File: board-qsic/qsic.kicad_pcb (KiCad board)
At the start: 4 copper layers, 214.1 x 131.7 mm, 152 parts, among them CON1 SD 0, CON2 SD 1, J601 USB_A, P2 Indicator Panel, U207 DS8641-LR, U208 74LVC8T245, U209 74LVC8T245, U210 DS8641-LR, U211 DS8641-LR, U212 74LVC8T245, U213 74LVC8T245, U214 DS8641-LR, U215 DS8641-LR, U216 74LVC8T245, U306 AOZ3010PI, U307 AOZ3010PI, U308 RT8288A, U309 SC189, U401 XC7A75T-CSG324, U501 IS43TR16128B, U502 DS8641-LR, U503 74LVC8T245, U504 74LVC8T245, U505 DS8641-LR, U506 DS8641-LR, U507 74LVC8T245, U508 74LVC8T245, U509 DS8641-LR, U510 DS8641-LR, U511 74LVC8T245, U512 74LVC8T245, U513 DS8641-LR, U601 MAX3033E, U602 USB3340

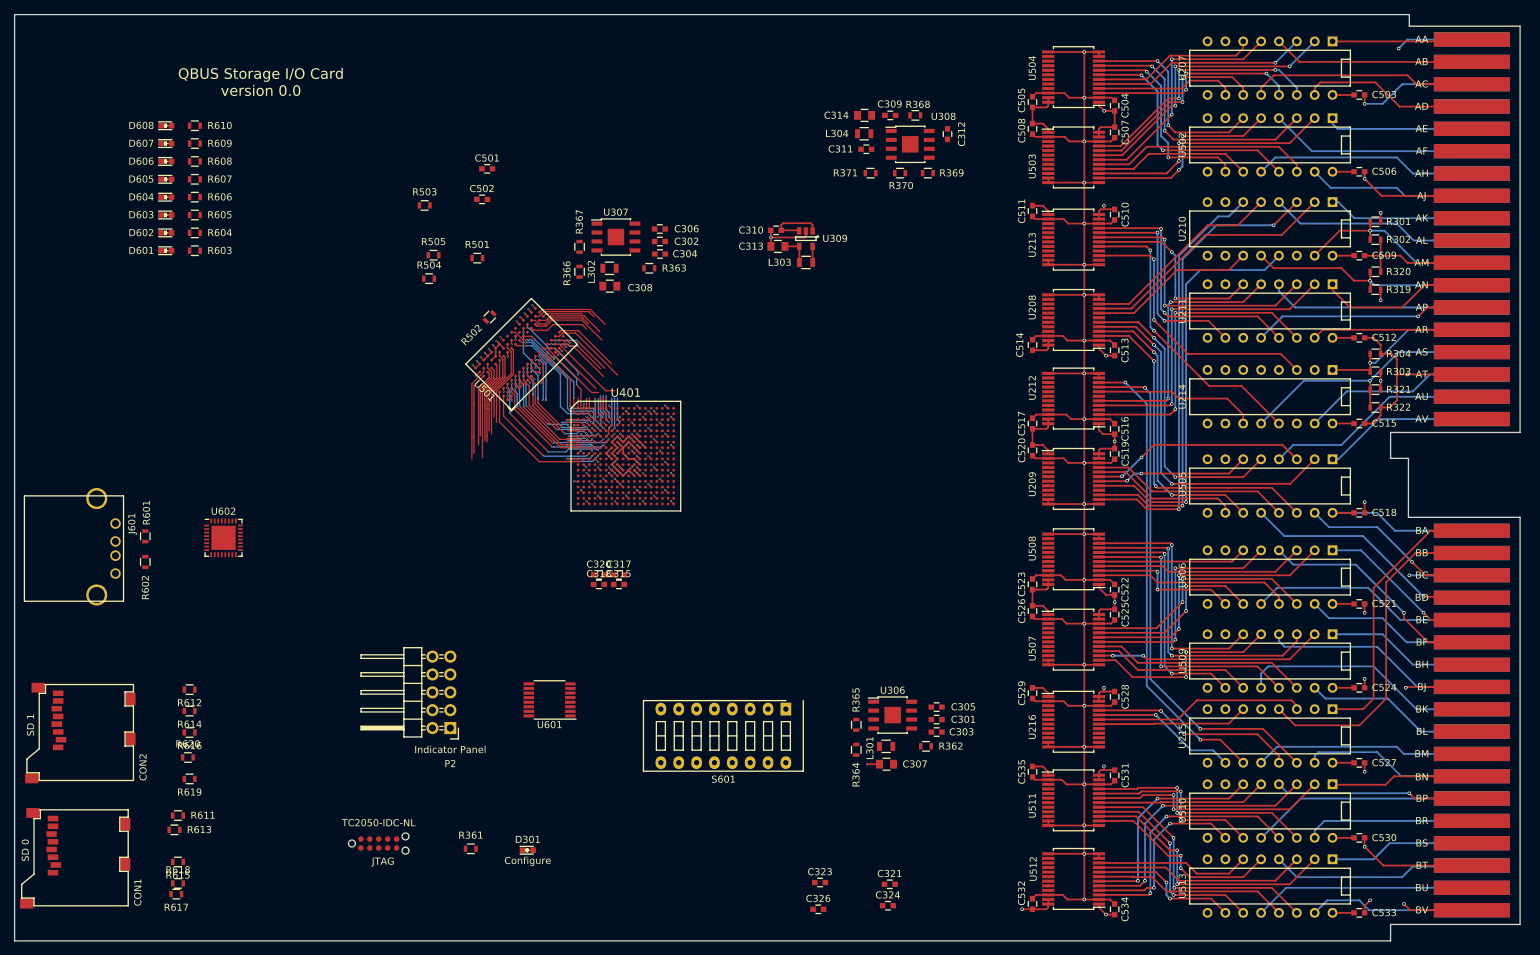
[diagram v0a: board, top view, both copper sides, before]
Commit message: Reworked board from template.  Changed schematic to let me use the bus drivers and level converters more efficiently so to get all the signals.
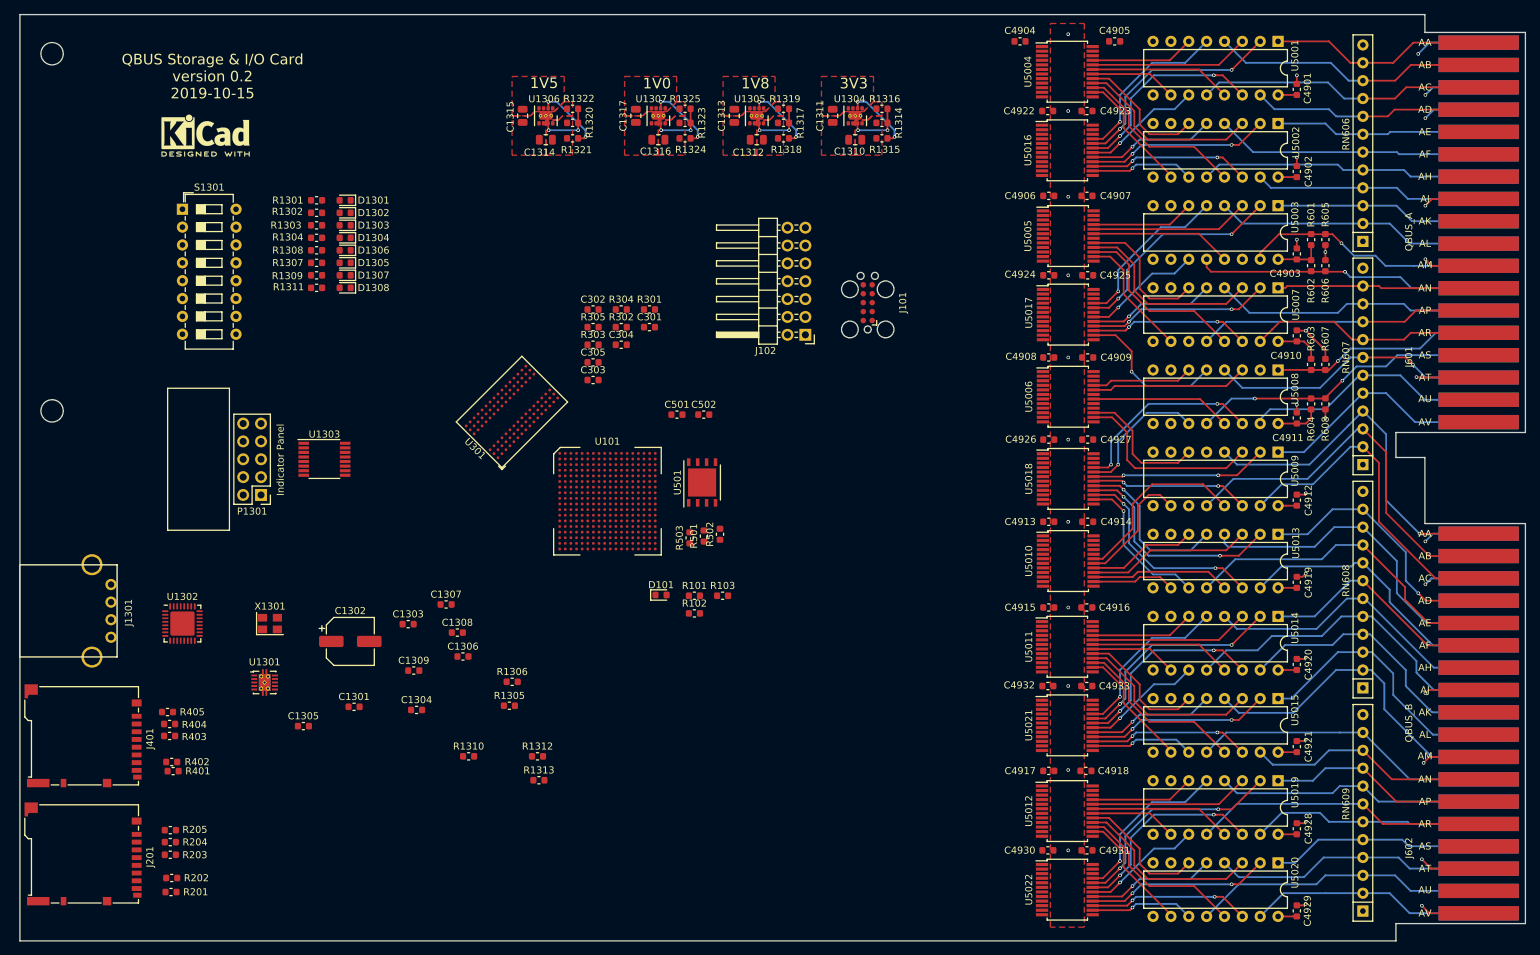
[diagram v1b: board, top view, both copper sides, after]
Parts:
- removed B101: QBUS, myMods.pretty:Qbus-double
- removed C306, C311, C312, C315, C317, C318, C320, C321, C323, C324, C326, C503, C504, C505, C506, C507, C508, C509, C510, C511, C512, C513, C514, C515, C516, C517, C518, C519, C520, C521, C522, C523, C524, C525, C526, C527, C528, C529, C530, C531, C532, C533, C534, C535: 100nF, Capacitors_SMD:C_0603
- removed C307, C308, C313, C314: 22uF, Capacitors_SMD:C_0805
- removed C309, C310: 10uF, Capacitors_SMD:C_0603
- removed CON1: SD 0, myMods.pretty:microSD-3M-2900-series
- removed CON2: SD 1, myMods.pretty:microSD-3M-2900-series
- removed D301: Configure, LEDs:LED-0603
- removed D601: LED 0, LEDs:LED-0603
- removed D602: LED 1, LEDs:LED-0603
- removed D603: LED 2, LEDs:LED-0603
- removed D604: LED 3, LEDs:LED-0603
- removed D605: LED 4, LEDs:LED-0603
- removed D606: LED 5, LEDs:LED-0603
- removed D607: LED 6, LEDs:LED-0603
- removed D608: LED 7, LEDs:LED-0603
- removed JTAG: TC2050-IDC-NL, myMods.pretty:TC2050-IDC-NL
- removed L301, L302: 4.7uH, Resistors_SMD:R_0805
- removed L303: 1.5uH, Resistors_SMD:R_0805
- removed L304: 2.2uH, Resistors_SMD:R_0805
- removed P2: Indicator Panel, Pin_Headers:Pin_Header_Angled_2x05
- removed R319, R321: 330, Resistors_SMD:R_0603
- removed R320, R322: 680, Resistors_SMD:R_0603
- removed R361, R505: 240, Resistors_SMD:R_0603
- removed R362, R363: 7.5k, Resistors_SMD:R_0603
- removed R364: 31.1k, Resistors_SMD:R_0603
- removed R365, R366: 10k, Resistors_SMD:R_0603
- removed R367: 11.5k, Resistors_SMD:R_0603
- removed R368: 100k, Resistors_SMD:R_0603
- removed R369, R611, R612, R613, R614, R615, R616, R617, R619: 50k, Resistors_SMD:R_0603
- removed R370: 18.2k, Resistors_SMD:R_0603
- removed R371: 4.7k, Resistors_SMD:R_0603
- removed R504: 47, Resistors_SMD:R_0603
- removed R609, R610: R, Resistors_SMD:R_0603
- removed R618, R620: 270k, Resistors_SMD:R_0603
- removed the REF** at (34.0, 55.9)
- removed S601: Config, Buttons_Switches_ThroughHole:SW_DIP_x8_Slide
- removed U207, U210, U211, U214, U215, U502, U505, U506, U509, U510, U513: DS8641-LR, Housings_DIP:DIP-16__300
- removed U208, U209, U212, U213, U216, U503, U504, U507, U508, U511, U512: 74LVC8T245, Housings_SSOP:SSOP-24_5.3x8.2mm_Pitch0.65mm
- removed U306, U307: AOZ3010PI, Housings_SOIC:SOIC-8-1EP_3.9x4.9mm_Pitch1.27mm
- removed U308: RT8288A, Housings_SOIC:SOIC-8-1EP_3.9x4.9mm_Pitch1.27mm
- removed U309: SC189, TO_SOT_Packages_SMD:SOT-23-5
- removed U401: XC7A75T-CSG324, myMods.pretty:CSG324
- removed U601: MAX3033E, Housings_SSOP:TSSOP-16_4.4x5mm_Pitch0.65mm
- removed U602: USB3340, Housings_DFN_QFN:QFN-32-1EP_5x5mm_Pitch0.5mm
- added C1301: 100nF, Capacitor_SMD:C_0603_1608Metric, F.Cu at (80.5, 123.9)
- added C1302: 150uF, Capacitor_SMD:CP_Elec_6.3x5.7, F.Cu at (80.0, 114.6)
- added C1303: 100nF, Capacitor_SMD:C_0603_1608Metric, F.Cu at (88.2, 112.1)
- added C1304: 100nF, Capacitor_SMD:C_0603_1608Metric, F.Cu at (89.4, 124.3)
- added C1305: 120uF, Capacitor_SMD:C_0603_1608Metric, F.Cu at (73.3, 126.6)
- added C1306: 1uF, Capacitor_SMD:C_0603_1608Metric, F.Cu at (96.0, 116.7)
- added C1307: 1uF, Capacitor_SMD:C_0603_1608Metric, F.Cu at (93.6, 109.3)
- added C1308: 10nF, Capacitor_SMD:C_0603_1608Metric, F.Cu at (95.2, 113.3)
- added C1309: 100nF, Capacitor_SMD:C_0603_1608Metric, F.Cu at (89.0, 118.7)
- added C1310: 22uF, Capacitor_SMD:C_0805_2012Metric, F.Cu at (151.8, 43.2)
- added C1311: 10uF, Capacitor_SMD:C_0805_2012Metric, F.Cu at (148.6, 39.8)
- added C1312: 22uF, Capacitor_SMD:C_0805_2012Metric, F.Cu at (137.8, 43.2)
- added C1313: 10uF, Capacitor_SMD:C_0805_2012Metric, F.Cu at (134.6, 39.8)
- added C1314: 22uF, Capacitor_SMD:C_0805_2012Metric, F.Cu at (107.8, 43.2)
- added C1315: 10uF, Capacitor_SMD:C_0805_2012Metric, F.Cu at (104.5, 39.8)
- added C1316: 22uF, Capacitor_SMD:C_0805_2012Metric, F.Cu at (123.8, 43.2)
- added C1317: 10uF, Capacitor_SMD:C_0805_2012Metric, F.Cu at (120.6, 39.8)
- added C4901: 100nF, Capacitor_SMD:C_0603_1608Metric, F.Cu at (214.6, 36.0)
- added C4902: 100nF, Capacitor_SMD:C_0603_1608Metric, F.Cu at (214.6, 47.7)
- added C4903: 100nF, Capacitor_SMD:C_0603_1608Metric, F.Cu at (214.6, 59.4)
- added C4904: 100nF, Capacitor_SMD:C_0603_1608Metric, F.Cu at (175.3, 29.2)
- added C4905: 100nF, Capacitor_SMD:C_0603_1608Metric, F.Cu at (188.7, 29.2)
- added C4906: 100nF, Capacitor_SMD:C_0603_1608Metric, F.Cu at (179.3, 51.2)
- added C4907: 100nF, Capacitor_SMD:C_0603_1608Metric, F.Cu at (184.8, 51.2)
- added C4908: 100nF, Capacitor_SMD:C_0603_1608Metric, F.Cu at (179.3, 74.2)
- added C4909: 100nF, Capacitor_SMD:C_0603_1608Metric, F.Cu at (184.9, 74.2)
- added C4910: 100nF, Capacitor_SMD:C_0603_1608Metric, F.Cu at (214.6, 71.1)
- added C4911: 100nF, Capacitor_SMD:C_0603_1608Metric, F.Cu at (214.6, 82.8)
- added C4912: 100nF, Capacitor_SMD:C_0603_1608Metric, F.Cu at (214.6, 94.5)
- added C4913: 100nF, Capacitor_SMD:C_0603_1608Metric, F.Cu at (179.3, 97.5)
- added C4914: 100nF, Capacitor_SMD:C_0603_1608Metric, F.Cu at (184.9, 97.5)
- added C4915: 100nF, Capacitor_SMD:C_0603_1608Metric, F.Cu at (179.3, 109.7)
- added C4916: 100nF, Capacitor_SMD:C_0603_1608Metric, F.Cu at (184.8, 109.7)
- added C4917: 100nF, Capacitor_SMD:C_0603_1608Metric, F.Cu at (179.3, 133.0)
- added C4918: 100nF, Capacitor_SMD:C_0603_1608Metric, F.Cu at (184.6, 133.0)
- added C4919: 100nF, Capacitor_SMD:C_0603_1608Metric, F.Cu at (214.6, 106.1)
- added C4920: 100nF, Capacitor_SMD:C_0603_1608Metric, F.Cu at (214.6, 117.8)
- added C4921: 100nF, Capacitor_SMD:C_0603_1608Metric, F.Cu at (214.6, 129.5)
- added C4922: 100nF, Capacitor_SMD:C_0603_1608Metric, F.Cu at (179.2, 39.1)
- added C4923: 100nF, Capacitor_SMD:C_0603_1608Metric, F.Cu at (184.8, 39.1)
- added C4924: 100nF, Capacitor_SMD:C_0603_1608Metric, F.Cu at (179.3, 62.5)
- added C4925: 100nF, Capacitor_SMD:C_0603_1608Metric, F.Cu at (184.9, 62.5)
- added C4926: 100nF, Capacitor_SMD:C_0603_1608Metric, F.Cu at (179.3, 85.9)
- added C4927: 100nF, Capacitor_SMD:C_0603_1608Metric, F.Cu at (184.9, 85.9)
- added C4928: 100nF, Capacitor_SMD:C_0603_1608Metric, F.Cu at (214.6, 141.2)
- added C4929: 100nF, Capacitor_SMD:C_0603_1608Metric, F.Cu at (214.6, 152.9)
- added C4930: 100nF, Capacitor_SMD:C_0603_1608Metric, F.Cu at (179.2, 144.3)
- added C4931: 100nF, Capacitor_SMD:C_0603_1608Metric, F.Cu at (184.8, 144.3)
- added C4932: 100nF, Capacitor_SMD:C_0603_1608Metric, F.Cu at (179.2, 120.9)
- added C4933: 100nF, Capacitor_SMD:C_0603_1608Metric, F.Cu at (184.8, 120.9)
- added D101: LED_ALT, LED_SMD:LED_0603_1608Metric, F.Cu at (124.2, 108.0)
- added D1301: green, LED_SMD:LED_0603_1608Metric, F.Cu at (79.3, 51.8)
- added D1302: green, LED_SMD:LED_0603_1608Metric, F.Cu at (79.3, 53.6)
- added D1303: green, LED_SMD:LED_0603_1608Metric, F.Cu at (79.3, 55.4)
- added D1304: green, LED_SMD:LED_0603_1608Metric, F.Cu at (79.3, 57.1)
- added D1305: green, LED_SMD:LED_0603_1608Metric, F.Cu at (79.3, 60.7)
- added D1306: green, LED_SMD:LED_0603_1608Metric, F.Cu at (79.3, 58.9)
- added D1307: green, LED_SMD:LED_0603_1608Metric, F.Cu at (79.3, 62.5)
- added D1308: green, LED_SMD:LED_0603_1608Metric, F.Cu at (79.3, 64.3)
- added J101: Conn_02x05_Odd_Even, Connector:Tag-Connect_TC2050-IDC-FP_2x05_P1.27mm_Vertical, F.Cu at (153.6, 66.4)
- added J102: Conn_02x07_Odd_Even, Connector_PinHeader_2.54mm:PinHeader_2x07_P2.54mm_Horizontal, F.Cu at (144.7, 70.9)
- added J1301: USB_A, myMods:USB-A-Amphenol-UE27, F.Cu at (46.0, 110.2)
- added J201: SD Card, Connector_Card:microSD_HC_Hirose_DM3BT-DSF-PEJS, F.Cu at (42.0, 144.8)
- added J401: SD Card, Connector_Card:microSD_HC_Hirose_DM3BT-DSF-PEJS, F.Cu at (42.0, 128.0)
- added J602: QBUS_B, DEC:DEC_Edge_Fingers_single_height, F.Cu at (234.4, 98.2)
- added LOGO101: Logo_Open_Hardware_Small, Symbol:KiCad-Logo2_5mm_SilkScreen, F.Cu at (59.4, 42.6)
- added P1301: Indicator Panel, myMods:Box_Header_2x05_P2.54mm, F.Cu at (67.3, 93.7)
- added R101: 240, Resistor_SMD:R_0603_1608Metric, F.Cu at (128.9, 108.1)
- added R102: 4.7k, Resistor_SMD:R_0603_1608Metric, F.Cu at (128.9, 110.6)
- added R103: 4.7k, Resistor_SMD:R_0603_1608Metric, F.Cu at (133.0, 108.1)
- added R1301: 240, Resistor_SMD:R_0603_1608Metric, F.Cu at (75.2, 51.8)
- added R1302: 240, Resistor_SMD:R_0603_1608Metric, F.Cu at (75.2, 53.6)
- added R1303: 240, Resistor_SMD:R_0603_1608Metric, F.Cu at (75.2, 55.4)
- added R1304: 240, Resistor_SMD:R_0603_1608Metric, F.Cu at (75.2, 57.1)
- added R1305: 100k, Resistor_SMD:R_0603_1608Metric, F.Cu at (102.6, 123.7)
- added R1306: 100k, Resistor_SMD:R_0603_1608Metric, F.Cu at (103.0, 120.3)
- added R1307: 240, Resistor_SMD:R_0603_1608Metric, F.Cu at (75.2, 60.7)
- added R1308: 240, Resistor_SMD:R_0603_1608Metric, F.Cu at (75.2, 58.9)
- added R1309: 240, Resistor_SMD:R_0603_1608Metric, F.Cu at (75.2, 62.5)
- added R1310: 56.2k, Resistor_SMD:R_0603_1608Metric, F.Cu at (96.8, 130.9)
- added R1311: 240, Resistor_SMD:R_0603_1608Metric, F.Cu at (75.2, 64.3)
- added R1312: 20k, Resistor_SMD:R_0603_1608Metric, F.Cu at (106.6, 130.9)
- added R1313: 8.06k, Resistor_SMD:R_0603_1608Metric, F.Cu at (106.8, 134.3)
- added R1314: 511k, Resistor_SMD:R_0603_1608Metric, F.Cu at (155.6, 40.8)
- added R1315: 499k, Resistor_SMD:R_0603_1608Metric, F.Cu at (155.6, 43.0)
- added R1316: 162k, Resistor_SMD:R_0603_1608Metric, F.Cu at (155.6, 38.8)
- added R1317: 200k, Resistor_SMD:R_0603_1608Metric, F.Cu at (141.6, 40.8)
- added R1318: 499k, Resistor_SMD:R_0603_1608Metric, F.Cu at (141.6, 43.0)
- added R1319: 162k, Resistor_SMD:R_0603_1608Metric, F.Cu at (141.6, 38.8)
- added R1320: 143k, Resistor_SMD:R_0603_1608Metric, F.Cu at (111.6, 40.8)
- added R1321: 499k, Resistor_SMD:R_0603_1608Metric, F.Cu at (111.6, 43.0)
- added R1322: 162k, Resistor_SMD:R_0603_1608Metric, F.Cu at (111.6, 38.8)
- added R1323: 40.2, Resistor_SMD:R_0603_1608Metric, F.Cu at (127.6, 40.8)
- added R1324: 499k, Resistor_SMD:R_0603_1608Metric, F.Cu at (127.6, 43.0)
- added R1325: 162k, Resistor_SMD:R_0603_1608Metric, F.Cu at (127.6, 38.8)
- added R201: 50k, Resistor_SMD:R_0603_1608Metric, F.Cu at (54.5, 150.2)
- added R202: 50k, Resistor_SMD:R_0603_1608Metric, F.Cu at (54.6, 148.2)
- added R203: 50k, Resistor_SMD:R_0603_1608Metric, F.Cu at (54.4, 144.9)
- added R204: 50k, Resistor_SMD:R_0603_1608Metric, F.Cu at (54.4, 143.1)
- added R205: 50k, Resistor_SMD:R_0603_1608Metric, F.Cu at (54.4, 141.4)
- added R305: 47, Resistor_SMD:R_0603_1608Metric, F.Cu at (114.5, 69.8)
- added R401: 50k, Resistor_SMD:R_0603_1608Metric, F.Cu at (54.8, 133.0)
- added R402: 50k, Resistor_SMD:R_0603_1608Metric, F.Cu at (54.6, 131.7)
- added R403: 50k, Resistor_SMD:R_0603_1608Metric, F.Cu at (54.3, 128.0)
- added R404: 50k, Resistor_SMD:R_0603_1608Metric, F.Cu at (54.3, 126.3)
- added R405: 50k, Resistor_SMD:R_0603_1608Metric, F.Cu at (54.0, 124.6)
- added REF**: DEC Handle, DEC:DEC-Handle, F.Cu at (33.0, 56.4)
- added REF**: mounting hole .125, DEC:mounting hole .125, F.Cu at (37.6, 31.0)
- added REF**: mounting hole .125, DEC:mounting hole .125, F.Cu at (37.6, 81.8)
- added RN606: 330/680, Resistor_THT:R_Array_SIP12, F.Cu at (224.0, 57.7)
- added RN607: 330/680, Resistor_THT:R_Array_SIP12, F.Cu at (224.0, 89.4)
- added RN608: 330/680, Resistor_THT:R_Array_SIP12, F.Cu at (224.0, 121.2)
- added RN609: 330/680, Resistor_THT:R_Array_SIP12, F.Cu at (224.0, 152.9)
- added S1301: Config, Button_Switch_THT:SW_DIP_SPSTx08_Slide_6.7x21.88mm_W7.62mm_P2.54mm_LowProfile, F.Cu at (56.1, 53.1)
- added U101: XC7A75T-CSG324, Package_BGA:BGA-324_15.0x15.0mm_Layout18x18_P0.8mm_Ball0.5mm_Pad0.4mm_NSMD, F.Cu at (116.6, 94.6)
- added U1301: TPS2561, Package_SON:VSON-10-1EP_3x3mm_P0.5mm_EP1.65x2.4mm_ThermalVias, F.Cu at (67.8, 120.4)
- added U1302: USB3340, Package_DFN_QFN:QFN-32-1EP_5x5mm_P0.5mm_EP3.45x3.45mm, F.Cu at (56.1, 112.0)
- added U1303: MAX3033E, Package_SO:TSSOP-16_4.4x5mm_P0.65mm, F.Cu at (76.3, 88.6)
- added U1304: TPS82085, Package_LGA:Texas_SIL0008D_MicroSiP-8-1EP_2.8x3mm_P0.65mm_EP1.1x1.9mm_ThermalVias, F.Cu at (151.8, 39.8)
- added U1305: TPS82085, Package_LGA:Texas_SIL0008D_MicroSiP-8-1EP_2.8x3mm_P0.65mm_EP1.1x1.9mm_ThermalVias, F.Cu at (137.8, 39.8)
- added U1306: TPS82085, Package_LGA:Texas_SIL0008D_MicroSiP-8-1EP_2.8x3mm_P0.65mm_EP1.1x1.9mm_ThermalVias, F.Cu at (107.8, 39.8)
- added U1307: TPS82085, Package_LGA:Texas_SIL0008D_MicroSiP-8-1EP_2.8x3mm_P0.65mm_EP1.1x1.9mm_ThermalVias, F.Cu at (123.8, 39.8)
- added U301: IS43TR16128B, Package_BGA:BGA-96_9.0x13.0mm_Layout2x3x16_P0.8mm, F.Cu at (103.0, 81.9)
- added U5001: DS8641-units, Package_DIP:DIP-16_W7.62mm, F.Cu at (212.0, 29.2)
- added U5002: DS8641-units, Package_DIP:DIP-16_W7.62mm, F.Cu at (212.0, 40.9)
- added U5003: DS8641-units, Package_DIP:DIP-16_W7.62mm, F.Cu at (212.0, 52.6)
- added U5004: 74LVC8T245-units, Package_SO:SSOP-24_5.3x8.2mm_P0.65mm, F.Cu at (182.0, 33.5)
- added U5005: 74LVC8T245-units, Package_SO:SSOP-24_5.3x8.2mm_P0.65mm, F.Cu at (182.1, 56.9)
- added U5006: 74LVC8T245-units, Package_SO:SSOP-24_5.3x8.2mm_P0.65mm, F.Cu at (182.1, 79.8)
- added U5007: DS8641-units, Package_DIP:DIP-16_W7.62mm, F.Cu at (212.0, 64.3)
- added U5008: DS8641-units, Package_DIP:DIP-16_W7.62mm, F.Cu at (212.0, 75.9)
- added U5009: DS8641-units, Package_DIP:DIP-16_W7.62mm, F.Cu at (212.0, 87.6)
- added U5010: 74LVC8T245-units, Package_SO:SSOP-24_5.3x8.2mm_P0.65mm, F.Cu at (182.1, 103.1)
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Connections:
- C301 pad 1: GND -> /Memory/1V5
- C301 pad 2: +5V -> GND
- C302 pad 1: GND -> /Memory/1V5
- C302 pad 2: +5V -> GND
- C303 pad 1: Net-(C303-Pad1) -> /Memory/1V5
- C304 pad 1: Net-(C304-Pad1) -> /Memory/1V5
- C304 pad 2: GND -> /Memory/VREF15
- C305 pad 1: Net-(C305-Pad1) -> /Memory/VREF15
- C501 pad 1: +1V5 -> /3V3
- C501 pad 2: /Memory/VREF15 -> GND
- C502 pad 1: /Memory/VREF15 -> /3V3
- R301 pad 1: +5V -> Net-(R301-Pad1)
- R301 pad 2: /Bus Transceivers/BIAKI -> GND
- R302 pad 1: /Bus Transceivers/BIAKI -> /Memory/CK#
- R302 pad 2: GND -> /Memory/CK
- R303 pad 1: +5V -> /Memory/RESET#
- R303 pad 2: /Bus Transceivers/BDMGI -> GND
- R304 pad 1: /Bus Transceivers/BDMGI -> /Memory/1V5
- R304 pad 2: GND -> /Memory/VREF15
- R501 pad 1: /Memory/RESET# -> /3V3
- R501 pad 2: GND -> Net-(R501-Pad2)
- R502 pad 1: /Memory/CK# -> /3V3
- R502 pad 2: /Memory/CK -> Net-(R502-Pad2)
- R503 pad 1: +1V5 -> /3V3
- R503 pad 2: /Memory/VREF15 -> Net-(R503-Pad2)
- R601 pad 1: /I/O/USB_D- -> /5V0
- R601 pad 2: GND -> /QBUS/QBUS-int/BIAKI
- R602 pad 1: /I/O/USB_D+ -> /5V0
- R602 pad 2: GND -> /QBUS/QBUS-int/BIAKO
- R603 pad 1: +3V3 -> /5V0
- R603 pad 2: Net-(D601-Pad2) -> /QBUS/QBUS-int/BDMGI
- R604 pad 1: +3V3 -> /5V0
- R604 pad 2: Net-(D602-Pad2) -> /QBUS/QBUS-int/BDMGO
- R605 pad 1: +3V3 -> /QBUS/QBUS-int/BIAKI
- R605 pad 2: Net-(D603-Pad2) -> GND
- R606 pad 1: +3V3 -> /QBUS/QBUS-int/BIAKO
- R606 pad 2: Net-(D604-Pad2) -> GND
- R607 pad 1: +3V3 -> /QBUS/QBUS-int/BDMGI
- R607 pad 2: Net-(D605-Pad2) -> GND
- R608 pad 1: +3V3 -> /QBUS/QBUS-int/BDMGO
- R608 pad 2: Net-(D606-Pad2) -> GND
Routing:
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- added copper zone on F.Cu, net /1V0
- added copper zone on F.Cu, net /1V5
- added copper zone on F.Cu, net /1V8
- added copper zone on F.Cu, net /3V3
- added copper zone on F.Cu, net /5V0
- added copper zone on Pwr.Cu, net /5V0
- added copper zone on F.Cu, net GND
- removed copper zone on Pwr.Cu, net +1V0
- removed copper zone on Pwr.Cu, net +1V5
- removed copper zone on Pwr.Cu, net +1V8
- removed copper zone on Pwr.Cu, net +3V3
- removed copper zone on Pwr.Cu, net +5V
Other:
- outline, holes or cut-outs redrawn
- board text added: "1V0"
- board text added: "1V5"
- board text added: "1V8"
- board text added: "3V3"
- board text added: "QBUS A"
- board text added: "QBUS B"
- board text added: "QBUS Storage & I/O Card version 0.2 2019-10-15"
- board text removed: "QBUS Storage I/O Card version 0.0"

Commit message: Design of prototype is done.  Needs checking before sending out.
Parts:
- removed C1301, C1303, C1304, C1309, C4901, C4902, C4903, C4904, C4905, C4906, C4907, C4908, C4909, C4910, C4911, C4912, C4913, C4914, C4915, C4916, C4917, C4918, C4919, C4920, C4921, C4922, C4923, C4924, C4925, C4926, C4927, C4928, C4929, C4930, C4931, C4932, C4933: 100nF, Capacitor_SMD:C_0603_1608Metric
- removed C1302: 150uF, Capacitor_SMD:CP_Elec_6.3x5.7
- removed C1305: 120uF, Capacitor_SMD:C_0603_1608Metric
- removed C1306, C1307: 1uF, Capacitor_SMD:C_0603_1608Metric
- removed C1308: 10nF, Capacitor_SMD:C_0603_1608Metric
- removed D1301, D1302, D1303, D1304, D1305, D1306, D1307, D1308: green, LED_SMD:LED_0603_1608Metric
- removed J1301: USB_A, myMods:USB-A-Amphenol-UE27
- removed J201, J401: SD Card, Connector_Card:microSD_HC_Hirose_DM3BT-DSF-PEJS
- removed P1301: Indicator Panel, myMods:Box_Header_2x05_P2.54mm
- removed R1301, R1302, R1303, R1304, R1307, R1308, R1309, R1311: 240, Resistor_SMD:R_0603_1608Metric
- removed R1305, R1306: 100k, Resistor_SMD:R_0603_1608Metric
- removed R1310: 56.2k, Resistor_SMD:R_0603_1608Metric
- removed R1312: 20k, Resistor_SMD:R_0603_1608Metric
- removed R1313: 8.06k, Resistor_SMD:R_0603_1608Metric
- removed R201, R202, R203, R204, R205, R401, R402, R403, R404, R405: 50k, Resistor_SMD:R_0603_1608Metric
- removed S1301: Config, Button_Switch_THT:SW_DIP_SPSTx08_Slide_6.7x21.88mm_W7.62mm_P2.54mm_LowProfile
- removed U1301: TPS2561, Package_SON:VSON-10-1EP_3x3mm_P0.5mm_EP1.65x2.4mm_ThermalVias
- removed U1302: USB3340, Package_DFN_QFN:QFN-32-1EP_5x5mm_P0.5mm_EP3.45x3.45mm
- removed U1303: MAX3033E, Package_SO:TSSOP-16_4.4x5mm_P0.65mm
- removed U5001, U5002, U5003, U5007, U5008, U5009, U5013, U5014, U5015, U5019, U5020: DS8641-units, Package_DIP:DIP-16_W7.62mm
- removed U5004, U5005, U5006, U5010, U5011, U5012, U5016, U5017, U5018, U5021, U5022: 74LVC8T245-units, Package_SO:SSOP-24_5.3x8.2mm_P0.65mm
- removed X1301: ASE-24.000MHz, Oscillator:Oscillator_SMD_Abracon_ASE-4Pin_3.2x2.5mm
- added C306: 100nF, Capacitor_SMD:C_0603_1608Metric, F.Cu at (137.2, 76.6)
- added C307: 100nF, Capacitor_SMD:C_0603_1608Metric, F.Cu at (120.5, 94.1)
- added C503: 100nF, Capacitor_SMD:C_0603_1608Metric, F.Cu at (101.5, 136.0)
- added C504: 150uF, Capacitor_SMD:CP_Elec_6.3x5.7, F.Cu at (78.5, 129.6)
- added C505: 100nF, Capacitor_SMD:C_0603_1608Metric, F.Cu at (59.8, 143.1)
- added C506: 100nF, Capacitor_SMD:C_0603_1608Metric, F.Cu at (48.6, 140.7)
- added C507: 100nF, Capacitor_SMD:C_0603_1608Metric, F.Cu at (93.3, 102.9)
- added C508: 100nF, Capacitor_SMD:C_0603_1608Metric, F.Cu at (129.8, 73.6)
- added C509: 1uF, Capacitor_SMD:C_0603_1608Metric, F.Cu at (50.5, 140.7)
- added C510: 1uF, Capacitor_SMD:C_0603_1608Metric, F.Cu at (57.9, 143.1)
- added C511: 10nF, Capacitor_SMD:C_0603_1608Metric, F.Cu at (51.3, 144.8)
- added C512: 100nF, Capacitor_SMD:C_0603_1608Metric, F.Cu at (130.8, 76.4)
- added C601: 100nF, Capacitor_SMD:C_0603_1608Metric, F.Cu at (214.6, 36.0)
- added C602: 100nF, Capacitor_SMD:C_0603_1608Metric, F.Cu at (214.6, 47.7)
- added C603: 100nF, Capacitor_SMD:C_0603_1608Metric, F.Cu at (214.6, 59.4)
- added C604: 100nF, Capacitor_SMD:C_0603_1608Metric, F.Cu at (214.6, 71.1)
- added C605: 100nF, Capacitor_SMD:C_0603_1608Metric, F.Cu at (214.6, 82.8)
- added C606: 100nF, Capacitor_SMD:C_0603_1608Metric, F.Cu at (214.6, 94.5)
- added C607: 100nF, Capacitor_SMD:C_0603_1608Metric, F.Cu at (214.6, 106.1)
- added C608: 100nF, Capacitor_SMD:C_0603_1608Metric, F.Cu at (214.6, 117.8)
- added C609: 100nF, Capacitor_SMD:C_0603_1608Metric, F.Cu at (214.6, 129.5)
- added C610: 100nF, Capacitor_SMD:C_0603_1608Metric, F.Cu at (214.6, 141.2)
- added C611: 100nF, Capacitor_SMD:C_0603_1608Metric, F.Cu at (214.6, 152.9)
- added C612: 100nF, Capacitor_SMD:C_0603_1608Metric, F.Cu at (189.0, 30.0)
- added C613: 100nF, Capacitor_SMD:C_0603_1608Metric, F.Cu at (185.1, 39.1)
- added C614: 100nF, Capacitor_SMD:C_0603_1608Metric, F.Cu at (185.1, 51.3)
- added C615: 100nF, Capacitor_SMD:C_0603_1608Metric, F.Cu at (185.1, 62.5)
- added C616: 100nF, Capacitor_SMD:C_0603_1608Metric, F.Cu at (185.1, 74.2)
- added C617: 100nF, Capacitor_SMD:C_0603_1608Metric, F.Cu at (185.1, 85.9)
- added C618: 100nF, Capacitor_SMD:C_0603_1608Metric, F.Cu at (185.1, 97.5)
- added C619: 100nF, Capacitor_SMD:C_0603_1608Metric, F.Cu at (185.1, 109.7)
- added C620: 100nF, Capacitor_SMD:C_0603_1608Metric, F.Cu at (185.1, 120.9)
- added C621: 100nF, Capacitor_SMD:C_0603_1608Metric, F.Cu at (185.1, 133.1)
- added C622: 100nF, Capacitor_SMD:C_0603_1608Metric, F.Cu at (185.1, 144.3)
- added C623: 100nF, Capacitor_SMD:C_0603_1608Metric, F.Cu at (175.2, 29.7)
- added C624: 100nF, Capacitor_SMD:C_0603_1608Metric, F.Cu at (179.1, 39.1)
- added C625: 100nF, Capacitor_SMD:C_0603_1608Metric, F.Cu at (179.1, 51.3)
- added C626: 100nF, Capacitor_SMD:C_0603_1608Metric, F.Cu at (179.1, 62.5)
- added C627: 100nF, Capacitor_SMD:C_0603_1608Metric, F.Cu at (179.1, 74.2)
- added C628: 100nF, Capacitor_SMD:C_0603_1608Metric, F.Cu at (179.1, 85.9)
- added C629: 100nF, Capacitor_SMD:C_0603_1608Metric, F.Cu at (179.1, 97.5)
- added C630: 100nF, Capacitor_SMD:C_0603_1608Metric, F.Cu at (179.1, 109.7)
- added C631: 100nF, Capacitor_SMD:C_0603_1608Metric, F.Cu at (179.1, 120.9)
- added C632: 100nF, Capacitor_SMD:C_0603_1608Metric, F.Cu at (179.1, 133.1)
- added C633: 100nF, Capacitor_SMD:C_0603_1608Metric, F.Cu at (179.1, 144.3)
- added D501: green, LED_SMD:LED_0603_1608Metric, F.Cu at (49.0, 62.2)
- added D502: green, LED_SMD:LED_0603_1608Metric, F.Cu at (49.0, 64.8)
- added D503: green, LED_SMD:LED_0603_1608Metric, F.Cu at (49.0, 67.3)
- added D504: green, LED_SMD:LED_0603_1608Metric, F.Cu at (49.0, 69.8)
- added D505: green, LED_SMD:LED_0603_1608Metric, F.Cu at (49.0, 72.4)
- added D506: green, LED_SMD:LED_0603_1608Metric, F.Cu at (49.0, 74.9)
- added D507: green, LED_SMD:LED_0603_1608Metric, F.Cu at (49.0, 77.5)
- added D508: green, LED_SMD:LED_0603_1608Metric, F.Cu at (49.0, 80.0)
- added J301: SD Card, Connector_Card:microSD_HC_Hirose_DM3BT-DSF-PEJS, F.Cu at (41.9, 99.2)
- added J302: SD Card, Connector_Card:microSD_HC_Hirose_DM3BT-DSF-PEJS, F.Cu at (41.9, 117.2)
- added J501: USB_A, myMods:USB-A-Amphenol-UE27, F.Cu at (46.0, 136.4)
- added P501: Indicator Panel, myMods:Box_Header_2x05_P2.54mm, F.Cu at (83.9, 99.1)
- added R306: 50k, Resistor_SMD:R_0603_1608Metric, F.Cu at (53.7, 104.6)
- added R307: 50k, Resistor_SMD:R_0603_1608Metric, F.Cu at (53.7, 102.6)
- added R308: 50k, Resistor_SMD:R_0603_1608Metric, F.Cu at (53.7, 99.4)
- added R309: 50k, Resistor_SMD:R_0603_1608Metric, F.Cu at (53.7, 97.5)
- added R310: 50k, Resistor_SMD:R_0603_1608Metric, F.Cu at (53.7, 95.6)
- added R311: 50k, Resistor_SMD:R_0603_1608Metric, F.Cu at (53.7, 122.3)
- added R312: 50k, Resistor_SMD:R_0603_1608Metric, F.Cu at (53.7, 120.4)
- added R313: 50k, Resistor_SMD:R_0603_1608Metric, F.Cu at (53.7, 117.5)
- added R314: 50k, Resistor_SMD:R_0603_1608Metric, F.Cu at (53.7, 115.6)
- added R315: 50k, Resistor_SMD:R_0603_1608Metric, F.Cu at (53.7, 113.7)
- added R504: 240, Resistor_SMD:R_0603_1608Metric, F.Cu at (52.9, 62.2)
- added R505: 240, Resistor_SMD:R_0603_1608Metric, F.Cu at (52.9, 64.8)
- added R506: 240, Resistor_SMD:R_0603_1608Metric, F.Cu at (52.9, 67.3)
- added R507: 240, Resistor_SMD:R_0603_1608Metric, F.Cu at (52.9, 69.8)
- added R508: 240, Resistor_SMD:R_0603_1608Metric, F.Cu at (52.9, 72.4)
- added R509: 240, Resistor_SMD:R_0603_1608Metric, F.Cu at (52.9, 74.9)
- added R510: 240, Resistor_SMD:R_0603_1608Metric, F.Cu at (52.9, 77.5)
- added R511: 240, Resistor_SMD:R_0603_1608Metric, F.Cu at (52.9, 80.0)
- added R512: 100k, Resistor_SMD:R_0603_1608Metric, F.Cu at (98.2, 138.5)
- added R513: 100k, Resistor_SMD:R_0603_1608Metric, F.Cu at (100.7, 131.6)
- added R514: 56.2k, Resistor_SMD:R_0603_1608Metric, F.Cu at (94.5, 133.2)
- added R515: 20k, Resistor_SMD:R_0603_1608Metric, F.Cu at (50.9, 133.1)
- added R516: 8.06k, Resistor_SMD:R_0603_1608Metric, F.Cu at (52.5, 140.7)
- added S501: Config, Button_Switch_THT:SW_DIP_SPSTx08_Slide_6.7x21.88mm_W7.62mm_P2.54mm_LowProfile, F.Cu at (66.0, 80.0)
- added U502: TPS2561, Package_SON:VSON-10-1EP_3x3mm_P0.5mm_EP1.65x2.4mm_ThermalVias, F.Cu at (97.9, 135.1)
- added U503: MAX3033E, Package_SO:TSSOP-16_4.4x5mm_P0.65mm, F.Cu at (91.1, 96.7)
- added U504: USB3340, Package_DFN_QFN:QFN-32-1EP_5x5mm_P0.5mm_EP3.45x3.45mm, F.Cu at (56.9, 137.3)
- added U601: DS8641-small, Package_DIP:DIP-16_W7.62mm, F.Cu at (212.0, 29.2)
- added U602: DS8641-small, Package_DIP:DIP-16_W7.62mm, F.Cu at (212.0, 40.9)
- added U603: DS8641-small, Package_DIP:DIP-16_W7.62mm, F.Cu at (212.0, 52.6)
- added U604: DS8641-small, Package_DIP:DIP-16_W7.62mm, F.Cu at (212.0, 64.3)
- added U605: DS8641-small, Package_DIP:DIP-16_W7.62mm, F.Cu at (212.0, 75.9)
- added U606: DS8641-small, Package_DIP:DIP-16_W7.62mm, F.Cu at (212.0, 87.6)
- added U607: DS8641-small, Package_DIP:DIP-16_W7.62mm, F.Cu at (212.0, 99.3)
- added U608: DS8641-small, Package_DIP:DIP-16_W7.62mm, F.Cu at (212.0, 111.0)
- added U609: DS8641-small, Package_DIP:DIP-16_W7.62mm, F.Cu at (212.0, 122.7)
- added U610: DS8641-small, Package_DIP:DIP-16_W7.62mm, F.Cu at (212.0, 134.4)
- added U611: DS8641-small, Package_DIP:DIP-16_W7.62mm, F.Cu at (212.0, 146.1)
- added U621: 74LVC8T245-small, Package_SO:SSOP-24_5.3x8.2mm_P0.65mm, F.Cu at (182.1, 33.5)
- added U622: 74LVC8T245-small, Package_SO:SSOP-24_5.3x8.2mm_P0.65mm, F.Cu at (182.1, 44.7)
- added U623: 74LVC8T245-small, Package_SO:SSOP-24_5.3x8.2mm_P0.65mm, F.Cu at (182.1, 56.9)
- added U624: 74LVC8T245-small, Package_SO:SSOP-24_5.3x8.2mm_P0.65mm, F.Cu at (182.1, 68.1)
- added U625: 74LVC8T245-small, Package_SO:SSOP-24_5.3x8.2mm_P0.65mm, F.Cu at (182.1, 79.8)
- added U626: 74LVC8T245-small, Package_SO:SSOP-24_5.3x8.2mm_P0.65mm, F.Cu at (182.1, 91.4)
- added U627: 74LVC8T245-small, Package_SO:SSOP-24_5.3x8.2mm_P0.65mm, F.Cu at (182.1, 103.1)
- added U628: 74LVC8T245-small, Package_SO:SSOP-24_5.3x8.2mm_P0.65mm, F.Cu at (182.1, 115.3)
- added U629: 74LVC8T245-small, Package_SO:SSOP-24_5.3x8.2mm_P0.65mm, F.Cu at (182.1, 126.5)
- added U630: 74LVC8T245-small, Package_SO:SSOP-24_5.3x8.2mm_P0.65mm, F.Cu at (182.1, 138.7)
- added U631: 74LVC8T245-small, Package_SO:SSOP-24_5.3x8.2mm_P0.65mm, F.Cu at (182.1, 149.9)
- added X501: ASE-24.000MHz, Oscillator:Oscillator_SMD_Abracon_ASE-4Pin_3.2x2.5mm, F.Cu at (54.6, 144.8)
- D101: value LED_ALT -> green
- J102: footprint Connector_PinHeader_2.54mm:PinHeader_2x07_P2.54mm_Horizontal -> Connector_PinHeader_2.00mm:PinHeader_2x07_P2.00mm_Vertical
- U501: value MT25Q-so8 -> MT25Q-mlq8
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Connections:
- net /QBUS/CCLK renamed /QBUS & I/O/CCLK
- net /QBUS/QBUS-int/BBS7 renamed /QBUS & I/O/QBUS-int/BBS7
- net /QBUS/QBUS-int/BDAL0 renamed /QBUS & I/O/QBUS-int/BDAL0
- net /QBUS/QBUS-int/BDAL1 renamed /QBUS & I/O/QBUS-int/BDAL1
- net /QBUS/QBUS-int/BDAL10 renamed /QBUS & I/O/QBUS-int/BDAL10
- net /QBUS/QBUS-int/BDAL11 renamed /QBUS & I/O/QBUS-int/BDAL11
- net /QBUS/QBUS-int/BDAL12 renamed /QBUS & I/O/QBUS-int/BDAL12
- net /QBUS/QBUS-int/BDAL13 renamed /QBUS & I/O/QBUS-int/BDAL13
- net /QBUS/QBUS-int/BDAL14 renamed /QBUS & I/O/QBUS-int/BDAL14
- net /QBUS/QBUS-int/BDAL15 renamed /QBUS & I/O/QBUS-int/BDAL15
- net /QBUS/QBUS-int/BDAL16 renamed /QBUS & I/O/QBUS-int/BDAL16
- net /QBUS/QBUS-int/BDAL17 renamed /QBUS & I/O/QBUS-int/BDAL17
- net /QBUS/QBUS-int/BDAL18 renamed /QBUS & I/O/QBUS-int/BDAL18
- net /QBUS/QBUS-int/BDAL19 renamed /QBUS & I/O/QBUS-int/BDAL19
- net /QBUS/QBUS-int/BDAL2 renamed /QBUS & I/O/QBUS-int/BDAL2
- net /QBUS/QBUS-int/BDAL20 renamed /QBUS & I/O/QBUS-int/BDAL20
- net /QBUS/QBUS-int/BDAL21 renamed /QBUS & I/O/QBUS-int/BDAL21
- net /QBUS/QBUS-int/BDAL3 renamed /QBUS & I/O/QBUS-int/BDAL3
- net /QBUS/QBUS-int/BDAL4 renamed /QBUS & I/O/QBUS-int/BDAL4
- net /QBUS/QBUS-int/BDAL5 renamed /QBUS & I/O/QBUS-int/BDAL5
- net /QBUS/QBUS-int/BDAL6 renamed /QBUS & I/O/QBUS-int/BDAL6
- net /QBUS/QBUS-int/BDAL7 renamed /QBUS & I/O/QBUS-int/BDAL7
- net /QBUS/QBUS-int/BDAL8 renamed /QBUS & I/O/QBUS-int/BDAL8
- net /QBUS/QBUS-int/BDAL9 renamed /QBUS & I/O/QBUS-int/BDAL9
- net /QBUS/QBUS-int/BDCOK renamed /QBUS & I/O/QBUS-int/BDCOK
- net /QBUS/QBUS-int/BDIN renamed /QBUS & I/O/QBUS-int/BDIN
- net /QBUS/QBUS-int/BDMGI renamed /QBUS & I/O/QBUS-int/BDMGI
- net /QBUS/QBUS-int/BDMGO renamed /QBUS & I/O/QBUS-int/BDMGO
- net /QBUS/QBUS-int/BDMR renamed /QBUS & I/O/QBUS-int/BDMR
- net /QBUS/QBUS-int/BDOUT renamed /QBUS & I/O/QBUS-int/BDOUT
- net /QBUS/QBUS-int/BEVNT renamed /QBUS & I/O/QBUS-int/BEVNT
- net /QBUS/QBUS-int/BHALT renamed /QBUS & I/O/QBUS-int/BHALT
- net /QBUS/QBUS-int/BIAKI renamed /QBUS & I/O/QBUS-int/BIAKI
- net /QBUS/QBUS-int/BIAKO renamed /QBUS & I/O/QBUS-int/BIAKO
- net /QBUS/QBUS-int/BINIT renamed /QBUS & I/O/QBUS-int/BINIT
- net /QBUS/QBUS-int/BIRQ4 renamed /QBUS & I/O/QBUS-int/BIRQ4
- net /QBUS/QBUS-int/BIRQ5 renamed /QBUS & I/O/QBUS-int/BIRQ5
- net /QBUS/QBUS-int/BIRQ6 renamed /QBUS & I/O/QBUS-int/BIRQ6
- net /QBUS/QBUS-int/BIRQ7 renamed /QBUS & I/O/QBUS-int/BIRQ7
- net /QBUS/QBUS-int/BPOK renamed /QBUS & I/O/QBUS-int/BPOK
- net /QBUS/QBUS-int/BREF renamed /QBUS & I/O/QBUS-int/BREF
- net /QBUS/QBUS-int/BRPLY renamed /QBUS & I/O/QBUS-int/BRPLY
- net /QBUS/QBUS-int/BSACK renamed /QBUS & I/O/QBUS-int/BSACK
- net /QBUS/QBUS-int/BSYNC renamed /QBUS & I/O/QBUS-int/BSYNC
- net /QBUS/QBUS-int/BWTBT renamed /QBUS & I/O/QBUS-int/BWTBT
- C301 pad 1: /Memory/1V5 -> /1V5
- C302 pad 1: /Memory/1V5 -> /1V5
- C303 pad 1: /Memory/1V5 -> /1V5
- C304 pad 1: /Memory/1V5 -> /1V5
- J101 pad 1: GND -> /3V3
- J102 pad 2: Net-(J102-Pad2) -> /3V3
- R304 pad 1: /Memory/1V5 -> /1V5
- U101 pad A10: (no net) -> Net-(U101-PadA10)
- U101 pad A11: Net-(U101-PadA11) -> /QBUS & I/O/RIRQ6
- U101 pad A13: Net-(U101-PadA13) -> /QBUS & I/O/RDAL17
- U101 pad A14: Net-(U101-PadA14) -> /QBUS & I/O/RRPLY
- U101 pad A15: Net-(U101-PadA15) -> /QBUS & I/O/RDOUT
- U101 pad A16: Net-(U101-PadA16) -> /QBUS & I/O/TIRQ5
- U101 pad A17: Net-(U101-PadA17) -> /3V3
- U101 pad A18: Net-(U101-PadA18) -> /QBUS & I/O/TDAL17
- U101 pad A7: /Memory/1V5 -> /1V5
- U101 pad A8: (no net) -> Net-(U101-PadA8)
- U101 pad A9: (no net) -> Net-(U101-PadA9)
- U101 pad B10: (no net) -> /1V8
- U101 pad B12: Net-(U101-PadB12) -> /QBUS & I/O/RIRQ5
- U101 pad B13: Net-(U101-PadB13) -> /QBUS & I/O/RDAL16
- U101 pad B16: Net-(U101-PadB16) -> /QBUS & I/O/RIRQ4
- U101 pad B17: Net-(U101-PadB17) -> /QBUS & I/O/TDAL16
- U101 pad B18: Net-(U101-PadB18) -> /QBUS & I/O/TRPLY
- U101 pad B8: (no net) -> Net-(U101-PadB8)
- U101 pad B9: (no net) -> Net-(U101-PadB9)
- U101 pad C10: (no net) -> Net-(U101-PadC10)
- U101 pad C11: (no net) -> Net-(U101-PadC11)
- U101 pad C13: Net-(U101-PadC13) -> /3V3
- U101 pad C15: Net-(U101-PadC15) -> /QBUS & I/O/TIRQ6
- U101 pad C16: Net-(U101-PadC16) -> /QBUS & I/O/RWTBT
- U101 pad C17: Net-(U101-PadC17) -> /QBUS & I/O/TDOUT
- U101 pad C3: /Memory/1V5 -> /1V5
- U101 pad C9: (no net) -> Net-(U101-PadC9)
- U101 pad D10: (no net) -> Net-(U101-PadD10)
- U101 pad D15: Net-(U101-PadD15) -> /QBUS & I/O/RSYNC
- U101 pad D16: Net-(U101-PadD16) -> /3V3
- U101 pad D17: Net-(U101-PadD17) -> /QBUS & I/O/TSYNC
- U101 pad D18: Net-(U101-PadD18) -> /QBUS & I/O/TDIN
- U101 pad D6: /Memory/1V5 -> /1V5
- U101 pad D9: (no net) -> Net-(U101-PadD9)
- U101 pad E15: Net-(U101-PadE15) -> /QBUS & I/O/RDIN
- U101 pad E16: Net-(U101-PadE16) -> /QBUS & I/O/RHALT
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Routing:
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- added copper zone on Pwr.Cu, net /1V0
- added copper zone on Pwr.Cu, net /1V5
- added copper zone on Pwr.Cu, net /1V8
- added copper zone on B.Cu, net /3V3
- added copper zone on Pwr.Cu, net /3V3
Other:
- board text added: "JTAG"
- board text added: "Loading"
- board text added: "TCK"
- board text added: "TDI"
- board text added: "TDO"
- board text added: "TMS"

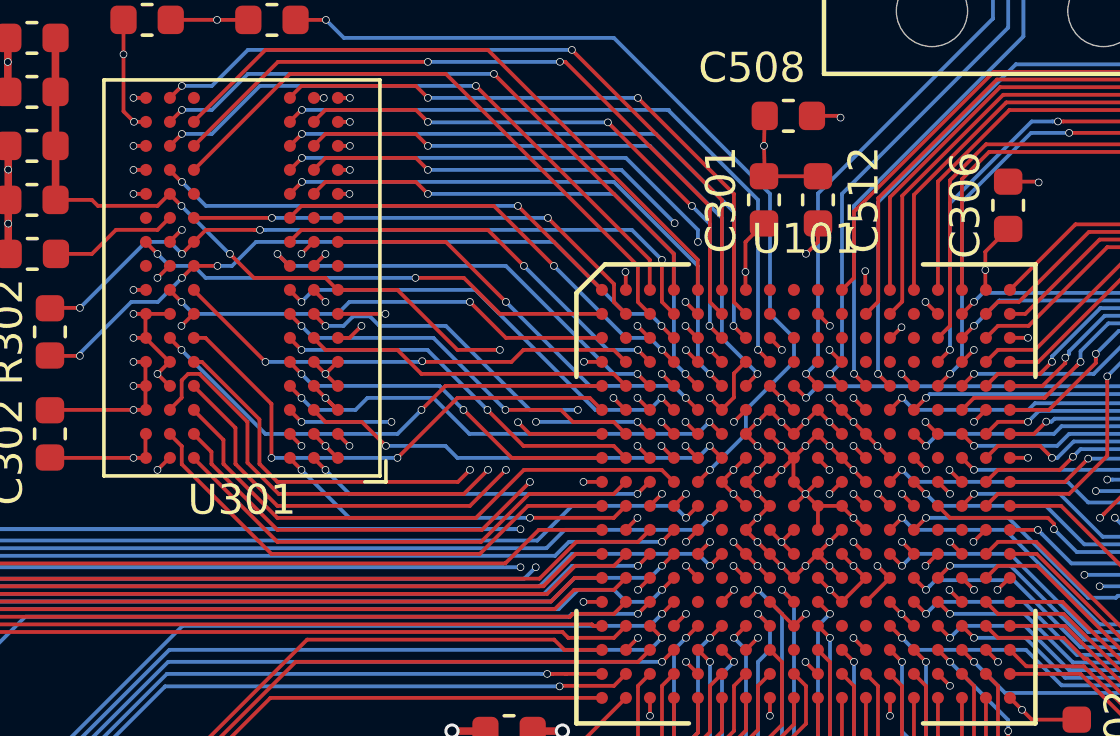
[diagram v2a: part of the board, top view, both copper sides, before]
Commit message: A few fixups from ERC.  Ground CS# on the memory chip.
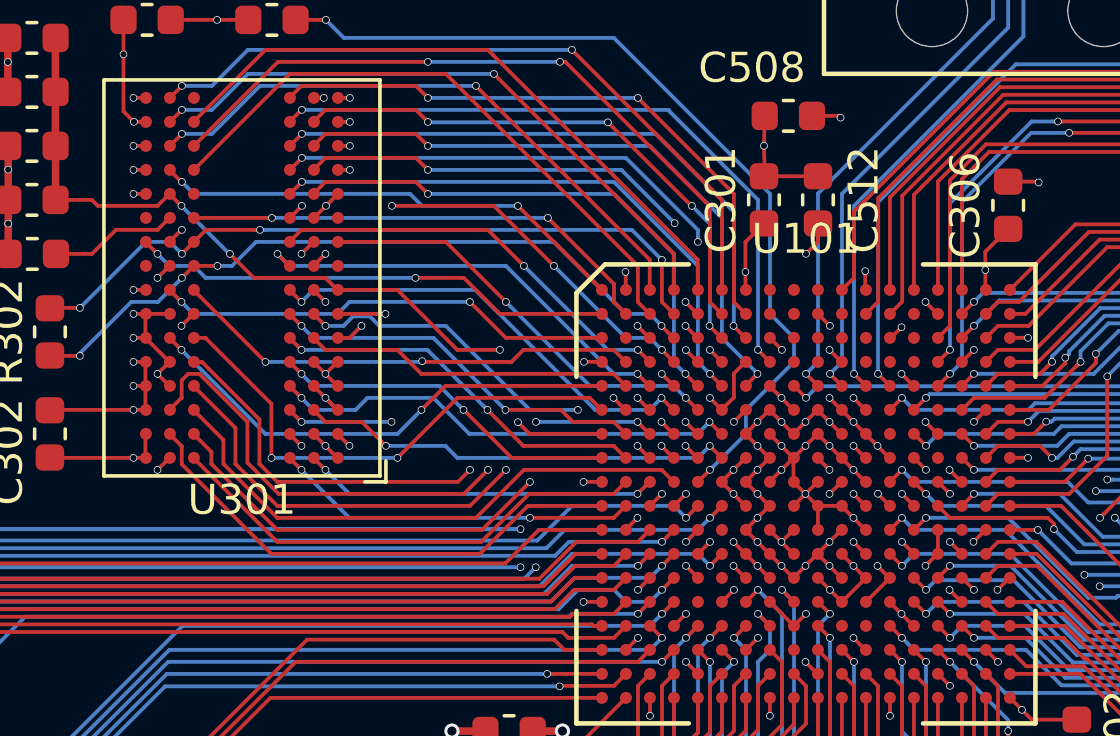
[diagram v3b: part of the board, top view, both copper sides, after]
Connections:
- net /QBUS & I/O/pin11 renamed Net-(U101-PadL6)
- U101 pad L15: Net-(U101-PadL15) -> GND
- U301 pad L2: Net-(U301-PadL2) -> GND
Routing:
- net GND: track 381.0 -> 382.5 mm
- net /Memory/WE#: track 15.1 -> 15.5 mm, vias 2 -> 4
